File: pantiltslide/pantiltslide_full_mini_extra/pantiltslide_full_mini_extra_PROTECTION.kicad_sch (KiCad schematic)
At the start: 81 parts, among them J1 Conn_01x22_Socket, J17 Motor_Slide, J18 Motor_Pan, J19 Motor_Tilt, J2 Conn_01x22_Socket, J20 TCA9548A_Mux, J21 AS5600_Pan, J22 AS5600_Tilt, J23 OLED, J24 TCA9548A_Mux, J26 Limit_Min, J27 Limit_Max, J28 Motor_Aux, J29 Enc_Slide, J3 MUX_2, J30 Enc_Pan, J31 Enc_Tilt, J32 Enc_Aux, J33 Btn_SetKeyframe, J34 Btn_ClearKeyframe, J35 Btn_PlayPause, J36 Btn_Reset, J37 5V_In, J38 24V_In, J4 MUX_3, J41 Aux_Max, J5 MUX_4, J6 MUX_5, J7 MUX_6, J8 MUX_7, U1 tmc2209, U2 tmc2209, U3 tmc2209, U4 tmc2209

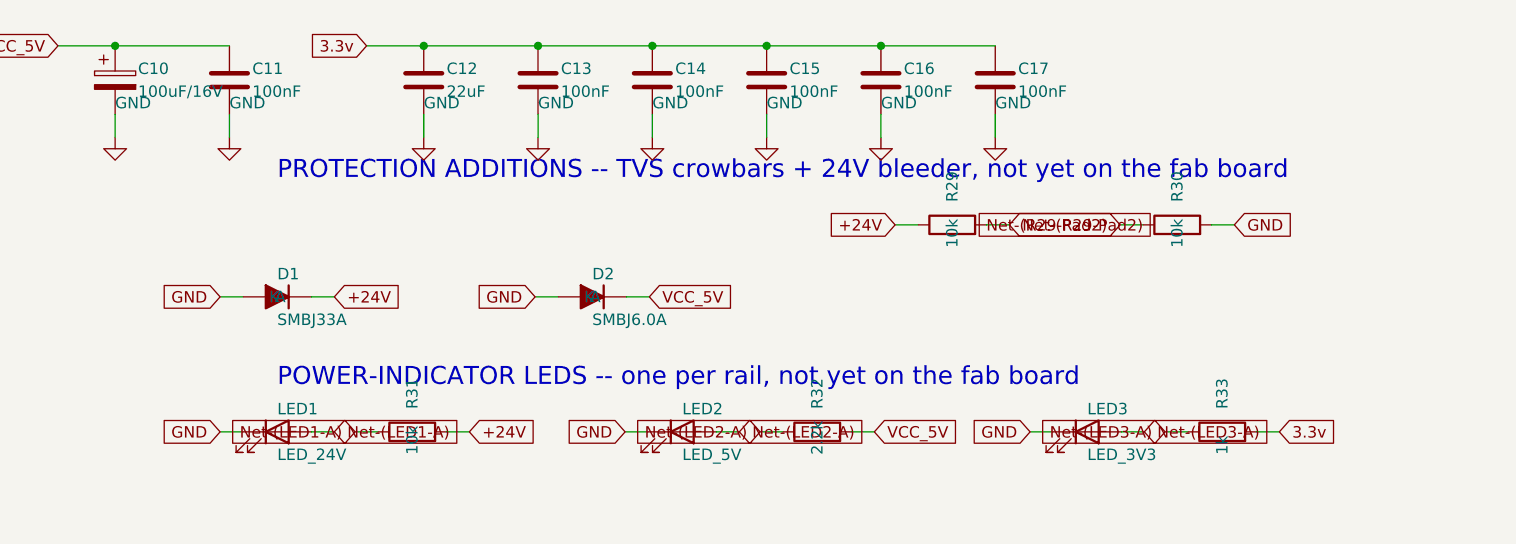
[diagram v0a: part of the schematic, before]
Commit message: formatting and spacing thing on the sch
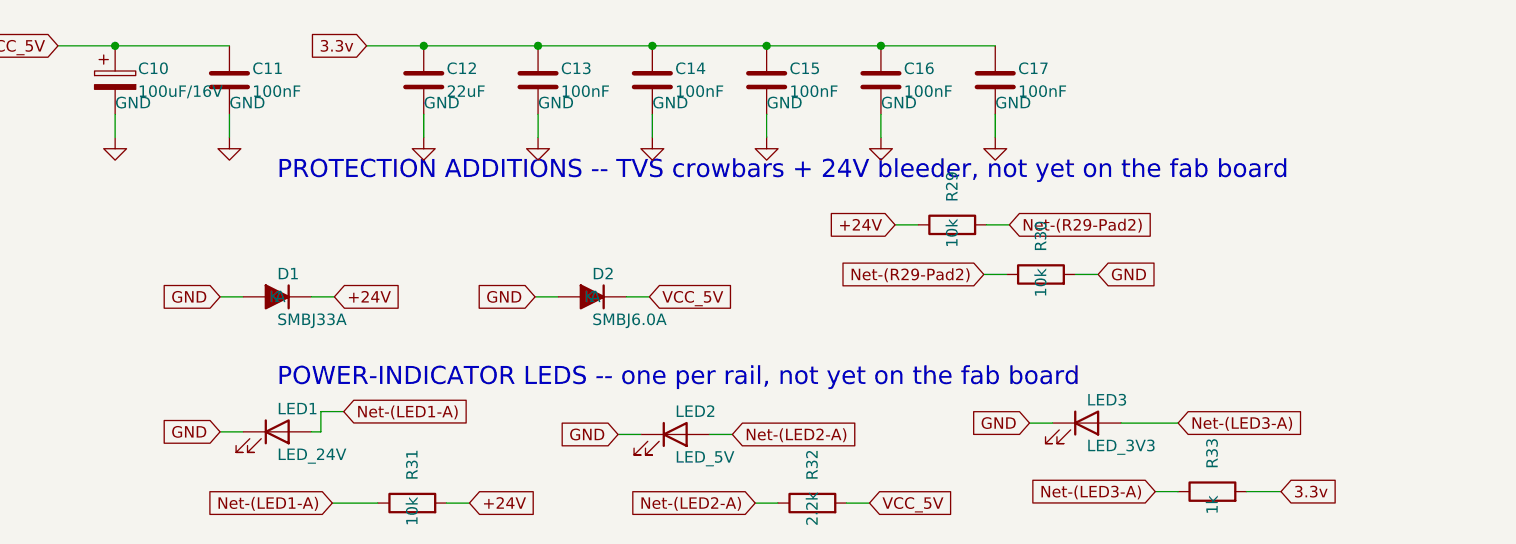
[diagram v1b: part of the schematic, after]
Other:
- moved on the sheet: LED2, LED3, R30, R31, R32, R33

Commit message: formatting
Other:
- note removed: "NEW ADDITIONS -- proposed pull-ups and filter caps, not yet on the fab board"
- moved on the sheet: C1, C10, C11, C12, C13, C14, C15, C16, C17, C2, C3, C4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
